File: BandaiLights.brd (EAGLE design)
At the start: 59.9 x 26.8 mm, 27 parts, among them Q1 FAN5333B, U1 AAAA-BATTERY, U2 AAAA-BATTERY

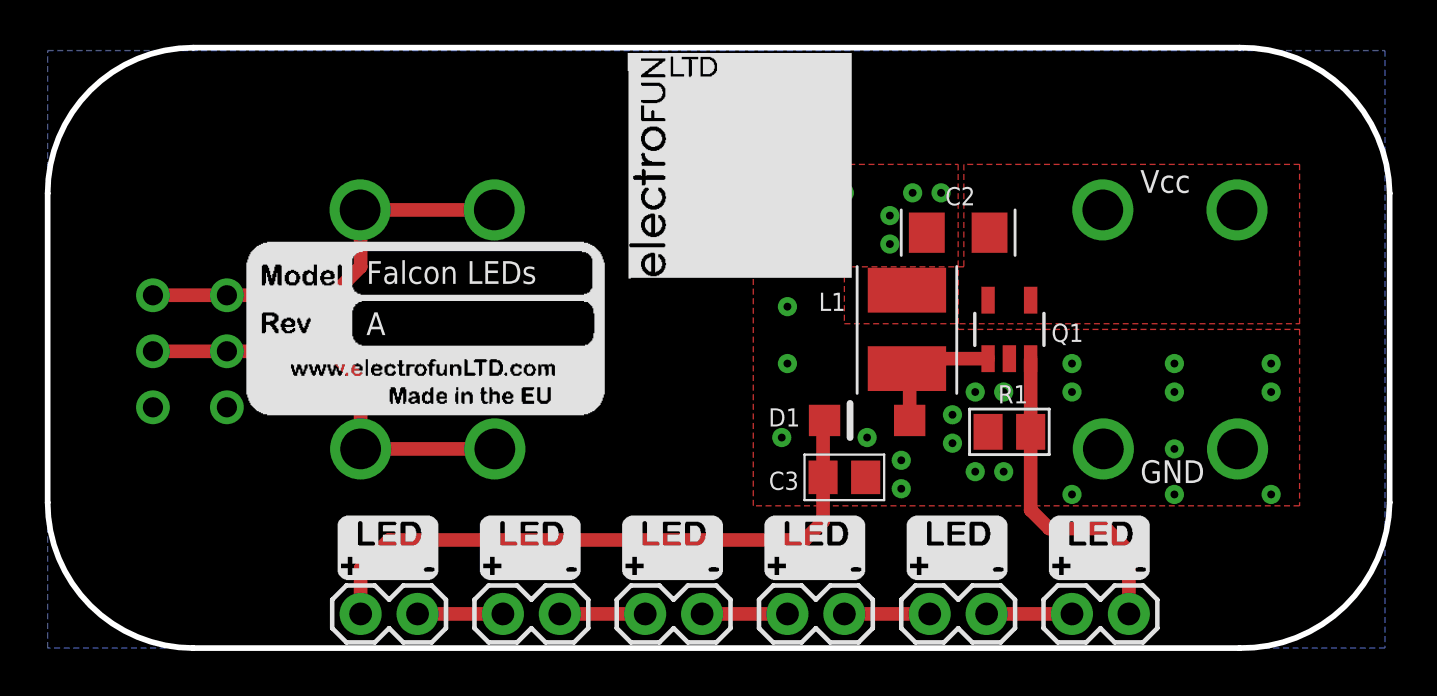
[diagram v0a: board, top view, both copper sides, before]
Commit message: Revised PCB: - Revised LED layout to avoid having to rework the interior of the Falcon to fit all 6 LEDs - Revised silk screen to make it more readable. - Added GK (geek kids logo).
Added license.
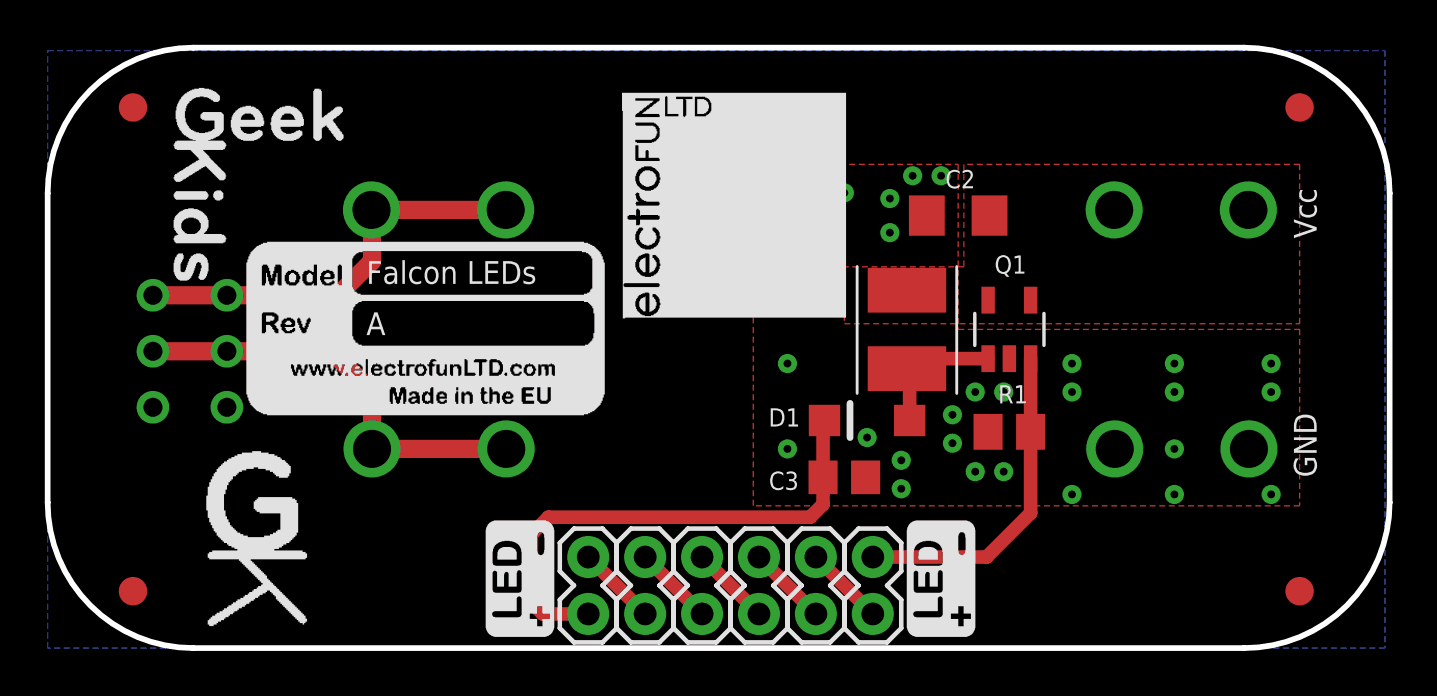
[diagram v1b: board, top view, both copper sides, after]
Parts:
- removed U$12, U$7: (no value), fmc:LED_SILK
- added TP1, TP2, TP3, TP4: TPB1,27, testpad:B1,27
- U$10: device fmc:LED_SILK -> fmc:GEEKKIDS_LOGO_S
- U$9: device fmc:LED_SILK -> fmc:GEEKKIDS_S
- moved U$9 26.1 mm to (5.59, 19.8)
- moved U$10 25.0 mm to (7.11, 1.02)
- moved LED1 10.2 mm to (24.1, 1.52), turned to 90 degrees
- moved LED6 8.89 mm to (36.8, 1.52), turned to 90 degrees
- moved LED2 6.35 mm to (26.7, 1.52), turned to 90 degrees
- moved LED5 5.08 mm to (34.3, 1.52), turned to 90 degrees
- moved U$8 4.17 mm to (22.6, 0.51), turned to 90 degrees
- moved U$11 3.97 mm to (41.4, 0.51), turned to 90 degrees
- moved LED3 2.54 mm to (29.2, 1.52), turned to 90 degrees
- moved U$3 1.80 mm to (25.7, 14.7)
- moved LED4 1.27 mm to (31.8, 1.52), turned to 90 degrees
- moved C2 0.76 mm to (40.6, 19.3)
- moved U1 0.51 mm to (53.6, 19.6)
- moved U2 0.51 mm to (14.5, 8.89)
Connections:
- net GND: now also U2.P3, U2.P4; no longer U2.P$3, U2.P$4
- net N$7: now also S1.P2, S1.P5, U2.P1, U2.P2; no longer S1.P$2, S1.P$5, U2.P$1, U2.P$2
- net N$8: now also S1.P1, S1.P4, U1.P3, U1.P4; no longer S1.P$1, S1.P$4, U1.P$3, U1.P$4
- net V+: now also U1.P1, U1.P2; no longer U1.P$1, U1.P$2
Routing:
- net VCC: track 28.6 -> 23.6 mm
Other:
- outline, holes or cut-outs redrawn

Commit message: Release Rev B, untested.
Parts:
- moved U$10 20.0 mm to (26.7, 5.33)
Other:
- board text added: "B"
- board text removed: "A"
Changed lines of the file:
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@@
 <?xml version="1.0" encoding="utf-8"?>
 <!DOCTYPE eagle SYSTEM "eagle.dtd">
-<eagle version="7.4.0">
+<eagle version="7.0.0">
 <drawing>
 <settings>
@@
 <layer number="21" name="tPlace" color="7" fill="1" visible="yes" active="yes"/>
 <layer number="22" name="bPlace" color="7" fill="1" visible="yes" active="yes"/>
-<layer number="23" name="tOrigins" color="15" fill="1" visible="no" active="yes"/>
+<layer number="23" name="tOrigins" color="15" fill="1" visible="yes" active="yes"/>
 <layer number="24" name="bOrigins" color="15" fill="1" visible="no" active="yes"/>
 <layer number="25" name="tNames" color="7" fill="1" visible="yes" active="yes"/>
@@
 <wire x1="6.5" y1="26.8" x2="0" y2="20.3" width="0.254" layer="20" curve="90"/>
 <text x="14.224" y="16.256" size="1.016" layer="21" font="vector" ratio="12">Falcon LEDs</text>
-<text x="14.224" y="13.97" size="1.016" layer="21" font="vector" ratio="12">A</text>
+<text x="14.224" y="13.97" size="1.016" layer="21" font="vector" ratio="12">B</text>
 <wire x1="35.814" y1="10.922" x2="35.814" y2="9.398" width="0.3048" layer="21"/>
 <text x="56.642" y="7.62" size="1.016" layer="21" font="vector" ratio="20" rot="R90">GND</text>
@@
 <attribute name="VALUE" x="55.245" y="1.778" size="0.0254" layer="27"/>
 </element>
-<element name="U$10" library="fmc" package="GEEKKIDS_LOGO_S" value="" x="7.112" y="1.016"/>
+<element name="U$10" library="fmc" package="GEEKKIDS_LOGO_S" value="" x="26.67" y="5.334"/>
 <element name="U$9" library="fmc" package="GEEKKIDS_S" value="" x="5.588" y="19.812"/>
 </elements>

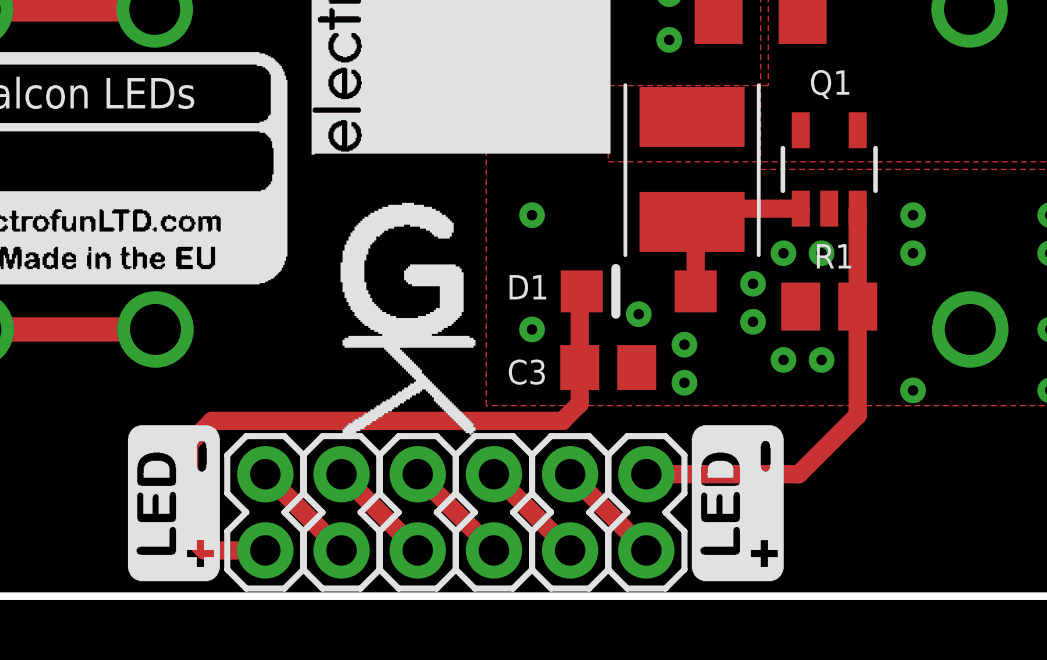
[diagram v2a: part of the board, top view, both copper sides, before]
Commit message: Updated LED setup to be in parallel.
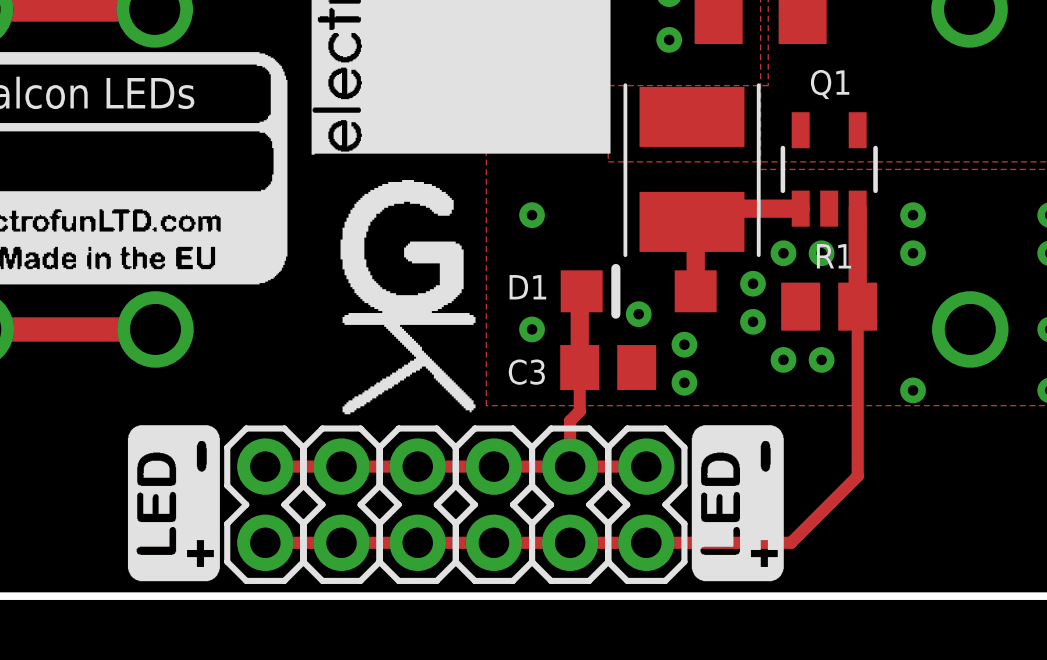
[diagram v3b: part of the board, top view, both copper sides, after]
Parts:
- moved LED1 2.79 mm to (24.1, 4.32), turned to 270 degrees
- moved LED2 2.79 mm to (26.7, 4.32), turned to 270 degrees
- moved LED3 2.79 mm to (29.2, 4.32), turned to 270 degrees
- moved LED4 2.79 mm to (31.8, 4.32), turned to 270 degrees
- moved LED5 2.79 mm to (34.3, 4.32), turned to 270 degrees
- moved LED6 2.79 mm to (36.8, 4.32), turned to 270 degrees
- moved U$10 0.76 mm to (26.7, 6.10)
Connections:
- removed net N$1: LED1.2, LED2.1
- removed net N$2: LED2.2, LED3.1
- removed net N$3: LED3.2, LED4.1
- removed net N$4: LED4.2, LED5.1
- removed net N$6: LED5.2, LED6.1
- net FB: now also LED1.2, LED2.2, LED3.2, LED4.2, LED5.2
- net VCC: now also LED2.1, LED3.1, LED4.1, LED5.1, LED6.1
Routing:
- net FB: track 14.7 -> 29.6 mm
- net VCC: track 23.6 -> 19.2 mm
- net N$1: track 3.59 -> 0.00 mm
- net N$6: track 3.59 -> 0.00 mm
- net N$4: track 3.59 -> 0.00 mm
- net N$3: track 3.59 -> 0.00 mm
- net N$2: track 3.59 -> 0.00 mm
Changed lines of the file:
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@@
 <?xml version="1.0" encoding="utf-8"?>
 <!DOCTYPE eagle SYSTEM "eagle.dtd">
-<eagle version="7.0.0">
+<eagle version="7.6.0">
 <drawing>
 <settings>
@@
 <layers>
 <layer number="1" name="Top" color="4" fill="1" visible="yes" active="yes"/>
+<layer number="2" name="Route2" color="1" fill="3" visible="no" active="yes"/>
+<layer number="15" name="Route15" color="4" fill="6" visible="no" active="yes"/>
 <layer number="16" name="Bottom" color="1" fill="1" visible="yes" active="yes"/>
 <layer number="17" name="Pads" color="2" fill="1" visible="yes" active="yes"/>
@@
 <layer number="20" name="Dimension" color="15" fill="1" visible="yes" active="yes"/>
 <layer number="21" name="tPlace" color="7" fill="1" visible="yes" active="yes"/>
-<layer number="22" name="bPlace" color="7" fill="1" visible="yes" active="yes"/>
+<layer number="22" name="bPlace" color="7" fill="1" visible="no" active="yes"/>
 <layer number="23" name="tOrigins" color="15" fill="1" visible="yes" active="yes"/>
-<layer number="24" name="bOrigins" color="15" fill="1" visible="no" active="yes"/>
+<layer number="24" name="bOrigins" color="15" fill="1" visible="yes" active="yes"/>
 <layer number="25" name="tNames" color="7" fill="1" visible="yes" active="yes"/>
 <layer number="26" name="bNames" color="7" fill="1" visible="no" active="yes"/>
@@
 <param name="mtCopper" value="0.035mm 0.035mm 0.035mm 0.035mm 0.035mm 0.035mm 0.035mm 0.035mm 0.035mm 0.035mm 0.035mm 0.035mm 0.035mm 0.035mm 0.035mm 0.035mm"/>
 <param name="mtIsolate" value="1.5mm 0.15mm 0.2mm 0.15mm 0.2mm 0.15mm 0.2mm 0.15mm 0.2mm 0.15mm 0.2mm 0.15mm 0.2mm 0.15mm 0.2mm"/>
-<param name="mdWireWire" value="8mil"/>
-<param name="mdWirePad" value="8mil"/>
-<param name="mdWireVia" value="8mil"/>
-<param name="mdPadPad" value="8mil"/>
-<param name="mdPadVia" value="8mil"/>
-<param name="mdViaVia" value="8mil"/>
-<param name="mdSmdPad" value="8mil"/>
-<param name="mdSmdVia" value="8mil"/>
-<param name="mdSmdSmd" value="8mil"/>
+<param name="mdWireWire" value="7mil"/>
+<param name="mdWirePad" value="7mil"/>
+<param name="mdWireVia" value="7mil"/>
+<param name="mdPadPad" value="7mil"/>
+<param name="mdPadVia" value="7mil"/>
+<param name="mdViaVia" value="7mil"/>
+<param name="mdSmdPad" value="7mil"/>
+<param name="mdSmdVia" value="7mil"/>
+<param name="mdSmdSmd" value="7mil"/>
 <param name="mdViaViaSameLayer" value="8mil"/>
 <param name="mnLayersViaInSmd" value="2"/>
@@
 <attribute name="VALUE" x="34.29" y="5.08" size="1.27" layer="27"/>
 </element>
-<element name="LED1" library="SparkFun" package="1X02" value="" x="24.13" y="1.524" smashed="yes" rot="R90">
-<attribute name="VALUE" x="27.305" y="0.254" size="1.27" layer="27" rot="R90"/>
-</element>
-<element name="LED2" library="SparkFun" package="1X02" value="" x="26.67" y="1.524" smashed="yes" rot="R90">
-<attribute name="VALUE" x="29.845" y="0.254" size="1.27" layer="27" rot="R90"/>
-</element>
-<element name="LED3" library="SparkFun" package="1X02" value="" x="29.21" y="1.524" smashed="yes" rot="R90">
-<attribute name="VALUE" x="32.385" y="0.254" size="1.27" layer="27" rot="R90"/>
-</element>
-<element name="LED4" library="SparkFun" package="1X02" value="" x="31.75" y="1.524" smashed="yes" rot="R90">
-<attribute name="VALUE" x="34.925" y="0.254" size="1.27" layer="27" rot="R90"/>
-</element>
-<element name="LED5" library="SparkFun" package="1X02" value="" x="34.29" y="1.524" smashed="yes" rot="R90">
-<attribute name="VALUE" x="37.465" y="0.254" size="1.27" layer="27" rot="R90"/>
-</element>
-<element name="LED6" library="SparkFun" package="1X02" value="" x="36.83" y="1.524" smashed="yes" rot="R90">
-<attribute name="VALUE" x="40.005" y="0.254" size="1.27" layer="27" rot="R90"/>
+<element name="LED1" library="SparkFun" package="1X02" value="" x="24.13" y="4.318" smashed="yes" rot="R270">
+<attribute name="VALUE" x="20.955" y="5.588" size="1.27" layer="27" rot="R270"/>
+</element>
+<element name="LED2" library="SparkFun" package="1X02" value="" x="26.67" y="4.318" smashed="yes" rot="R270">
+<attribute name="VALUE" x="23.495" y="5.588" size="1.27" layer="27" rot="R270"/>
+</element>
+<element name="LED3" library="SparkFun" package="1X02" value="" x="29.21" y="4.318" smashed="yes" rot="R270">
+<attribute name="VALUE" x="26.035" y="5.588" size="1.27" layer="27" rot="R270"/>
+</element>
+<element name="LED4" library="SparkFun" package="1X02" value="" x="31.75" y="4.318" smashed="yes" rot="R270">
+<attribute name="VALUE" x="28.575" y="5.588" size="1.27" layer="27" rot="R270"/>
+</element>
+<element name="LED5" library="SparkFun" package="1X02" value="" x="34.29" y="4.318" smashed="yes" rot="R270">
+<attribute name="VALUE" x="31.115" y="5.588" size="1.27" layer="27" rot="R270"/>
+</element>
+<element name="LED6" library="SparkFun" package="1X02" value="" x="36.83" y="4.318" smashed="yes" rot="R270">
+<attribute name="VALUE" x="33.655" y="5.588" size="1.27" layer="27" rot="R270"/>
 </element>
 <element name="U$3" library="fmc" package="ELECTROFUN_10X10" value="" x="25.654" y="14.732"/>
@@
 <attribute name="VALUE" x="55.245" y="1.778" size="0.0254" layer="27"/>
 </element>
-<element name="U$10" library="fmc" package="GEEKKIDS_LOGO_S" value="" x="26.67" y="5.334"/>
+<element name="U$10" library="fmc" package="GEEKKIDS_LOGO_S" value="" x="26.67" y="6.096"/>
 <element name="U$9" library="fmc" package="GEEKKIDS_S" value="" x="5.588" y="19.812"/>
 </elements>
@@
 <contactref element="R1" pad="2"/>
 <contactref element="Q1" pad="3"/>
+<wire x1="43.876" y1="12.918" x2="43.876" y2="9.652" width="0.6096" layer="1"/>
+<contactref element="LED2" pad="2"/>
+<contactref element="LED4" pad="2"/>
 <contactref element="LED6" pad="2"/>
-<wire x1="43.876" y1="12.918" x2="43.876" y2="9.652" width="0.6096" layer="1"/>
-<wire x1="43.876" y1="9.652" x2="43.876" y2="6.03" width="0.6096" layer="1"/>
-<wire x1="43.876" y1="6.03" x2="41.91" y2="4.064" width="0.6096" layer="1"/>
-<wire x1="41.91" y1="4.064" x2="36.83" y2="4.064" width="0.6096" layer="1"/>
+<contactref element="LED1" pad="2"/>
+<contactref element="LED5" pad="2"/>
+<contactref element="LED3" pad="2"/>
+<wire x1="24.13" y1="1.778" x2="26.67" y2="1.778" width="0.4064" layer="1"/>
+<wire x1="26.67" y1="1.778" x2="29.21" y2="1.778" width="0.4064" layer="1"/>
+<wire x1="29.21" y1="1.778" x2="31.75" y2="1.778" width="0.4064" layer="1"/>
+<wire x1="31.75" y1="1.778" x2="34.29" y2="1.778" width="0.4064" layer="1"/>
+<wire x1="34.29" y1="1.778" x2="36.83" y2="1.778" width="0.4064" layer="1"/>
+<wire x1="36.83" y1="1.778" x2="41.656" y2="1.778" width="0.4064" layer="1"/>
+<wire x1="41.656" y1="1.778" x2="43.876" y2="3.998" width="0.4064" layer="1"/>
+<wire x1="43.876" y1="9.652" x2="43.876" y2="3.998" width="0.4064" layer="1"/>
 </signal>
 <signal name="VCC">
@@
 <wire x1="34.676" y1="10.16" x2="34.61" y2="10.414" width="0.6096" layer="1"/>
 <wire x1="34.61" y1="10.414" x2="34.61" y2="7.62" width="0.6096" layer="1"/>
-<wire x1="34.61" y1="7.62" x2="34.61" y2="6.416" width="0.6096" layer="1"/>
-<wire x1="34.61" y1="6.416" x2="34.036" y2="5.842" width="0.6096" layer="1"/>
-<wire x1="34.036" y1="5.842" x2="22.352" y2="5.842" width="0.6096" layer="1"/>
-<wire x1="22.352" y1="5.842" x2="21.59" y2="5.08" width="0.6096" layer="1"/>
-<wire x1="21.59" y1="5.08" x2="21.59" y2="2.032" width="0.6096" layer="1"/>
-<wire x1="21.59" y1="2.032" x2="22.098" y2="1.524" width="0.6096" layer="1"/>
-<wire x1="22.098" y1="1.524" x2="24.13" y2="1.524" width="0.6096" layer="1"/>
-</signal>
-<signal name="N$1">
-<contactref element="LED1" pad="2"/>
+<contactref element="LED3" pad="1"/>
+<contactref element="LED5" pad="1"/>
+<contactref element="LED4" pad="1"/>
+<contactref element="LED6" pad="1"/>
 <contactref element="LED2" pad="1"/>
-<wire x1="24.13" y1="4.064" x2="26.67" y2="1.524" width="0.6096" layer="1"/>
-</signal>
-<signal name="N$2">
-<contactref element="LED2" pad="2"/>
-<contactref element="LED3" pad="1"/>
-<wire x1="26.67" y1="4.064" x2="29.21" y2="1.524" width="0.6096" layer="1"/>
-</signal>
-<signal name="N$3">
-<contactref element="LED3" pad="2"/>
-<contactref element="LED4" pad="1"/>
-<wire x1="29.21" y1="4.064" x2="31.75" y2="1.524" width="0.6096" layer="1"/>
-</signal>
-<signal name="N$4">
-<contactref element="LED4" pad="2"/>
-<contactref element="LED5" pad="1"/>
-<wire x1="31.75" y1="4.064" x2="34.29" y2="1.524" width="0.6096" layer="1"/>
-</signal>
-<signal name="N$6">
-<contactref element="LED5" pad="2"/>
-<contactref element="LED6" pad="1"/>
-<wire x1="34.29" y1="4.064" x2="36.83" y2="1.524" width="0.6096" layer="1"/>
+<wire x1="34.61" y1="7.62" x2="34.61" y2="6.162" width="0.4064" layer="1"/>
+<wire x1="34.61" y1="6.162" x2="34.29" y2="5.842" width="0.4064" layer="1"/>
+<wire x1="34.29" y1="5.842" x2="34.29" y2="4.318" width="0.4064" layer="1"/>
+<wire x1="36.83" y1="4.318" x2="34.29" y2="4.318" width="0.4064" layer="1"/>
+<wire x1="34.29" y1="4.318" x2="31.75" y2="4.318" width="0.4064" layer="1"/>
+<wire x1="31.75" y1="4.318" x2="29.21" y2="4.318" width="0.4064" layer="1"/>
+<wire x1="29.21" y1="4.318" x2="26.67" y2="4.318" width="0.4064" layer="1"/>
+<wire x1="26.67" y1="4.318" x2="24.13" y2="4.318" width="0.4064" layer="1"/>
 </signal>
 <signal name="N$7">
